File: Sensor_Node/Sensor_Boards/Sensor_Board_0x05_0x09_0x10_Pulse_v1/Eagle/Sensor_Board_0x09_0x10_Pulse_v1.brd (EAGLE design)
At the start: 55 x 35 mm, 21 parts, among them J3 1x3 RA Female .1", J4 ARDUINO_ISP, J6 1x3 RA Female .1", U2 ATMEGA328P_TQFP, Y1 8MHZ

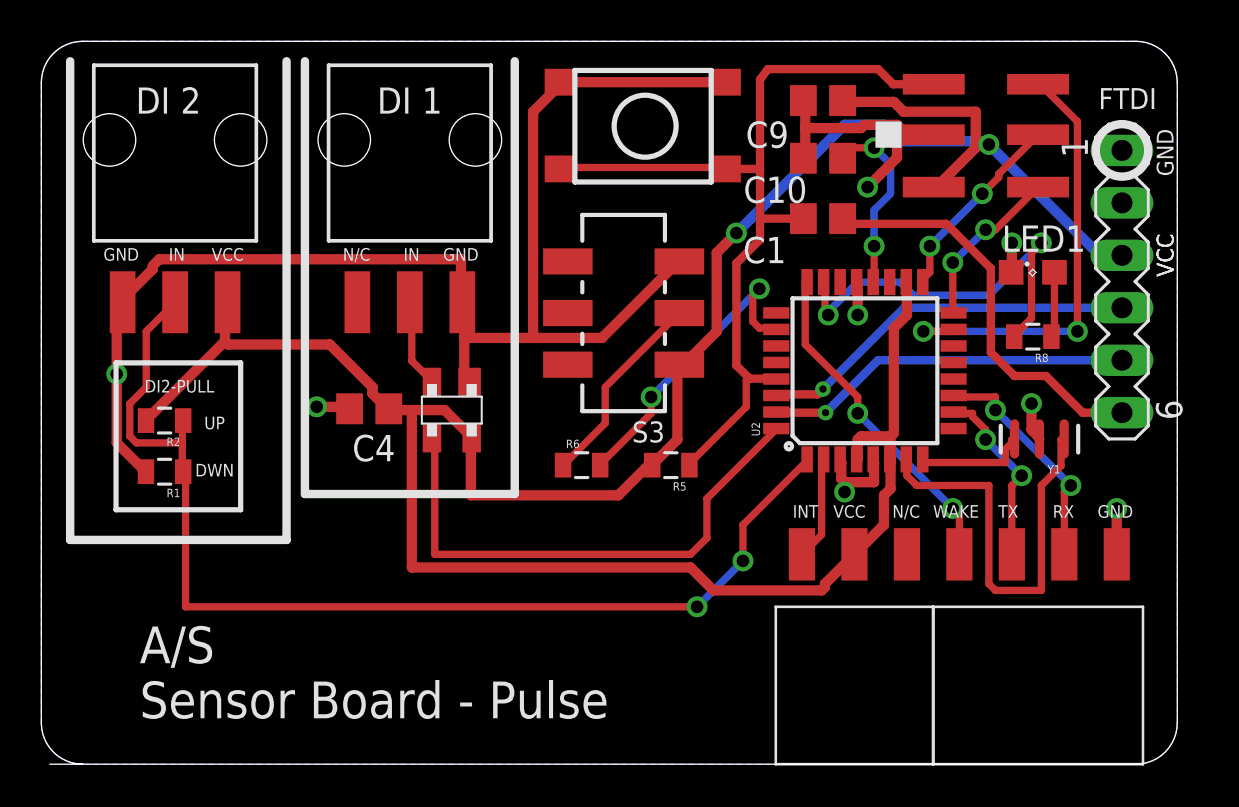
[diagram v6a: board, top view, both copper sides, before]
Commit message: Changes on PulseBoard
- startet replacement and rerouting
- corrected faulty VCC-Connection
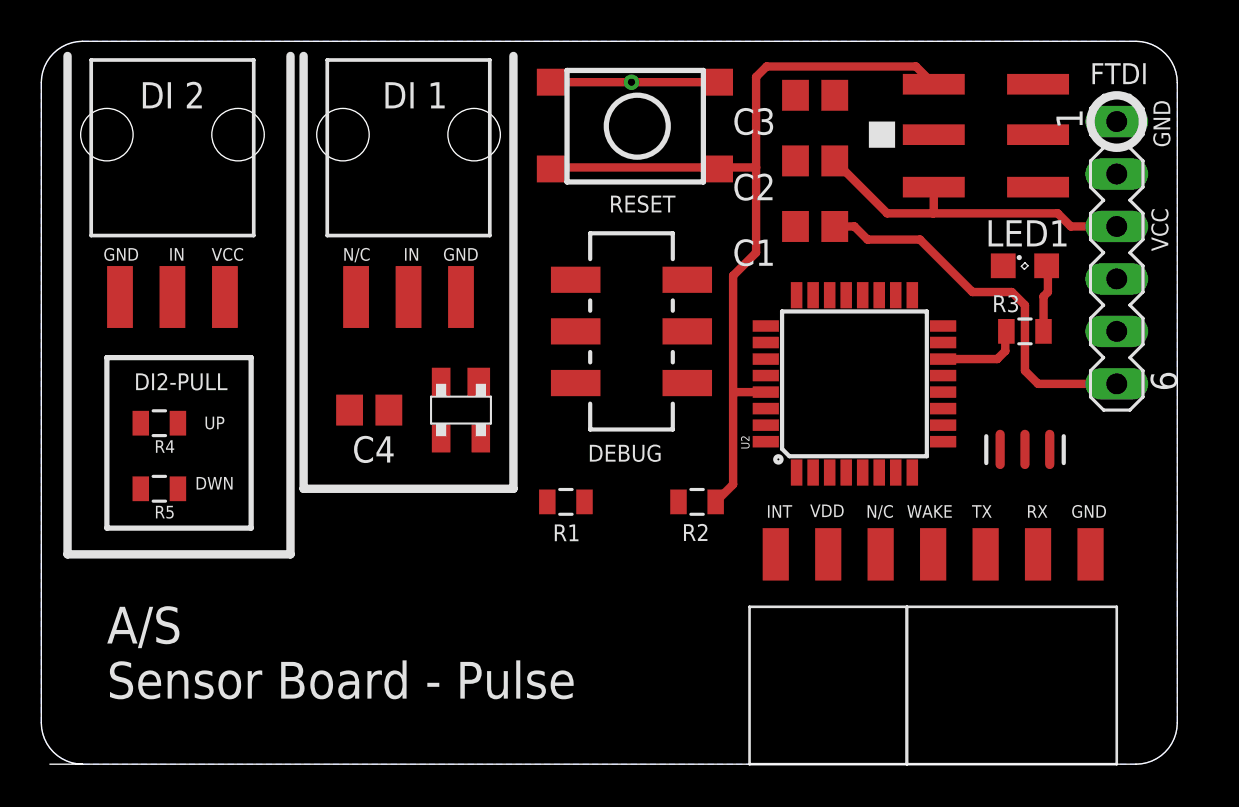
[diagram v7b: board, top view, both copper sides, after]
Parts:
- removed C10, C9: 100n, eagle-ltspice:C0805
- removed J3, J6: 1x3 RA Female .1", SparkFun-Connectors:1X03_SMD_RA_FEMALE
- removed R6: 10k, SparkFun-Passives:0805
- removed R8: 330, SparkFun-Passives:0805
- removed U$15: M03_SMD_90, myownthings:M03_SMD_90
- removed U$16: M04_SMD_90, myownthings:M04_SMD_90
- added C2, C3: 100n, eagle-ltspice:C0805
- added R3: 330, SparkFun-Passives:0805
- added R4: 10k, SparkFun-Passives:0805
- added SV2: M03_SMD_90, myownthings:M03_SMD_90
- added SV3: M04_SMD_90, myownthings:M04_SMD_90
- added SV4, SV5: 1x3 RA Female .1", SparkFun-Connectors:1X03_SMD_RA_FEMALE
- moved R2 26.1 mm to (31.8, 12.7)
- moved R5 24.8 mm to (5.71, 13.3)
- moved R1 19.5 mm to (25.4, 12.7), turned to 0 degrees
- moved SV1 1.42 mm to (52.1, 24.8)
- moved S3 0.97 mm to (28.6, 21.0)
- moved Y1 0.86 mm to (47.6, 15.2)
- moved U2 0.81 mm to (39.4, 18.4)
- moved C1 0.54 mm to (37.5, 26.0)
- moved LED1 0.50 mm to (47.6, 24.1)
- moved U$2 0.44 mm to (20.3, 17.1)
- moved S1 0.38 mm to (24.8, 33.0)
- moved C4 0.06 mm to (15.9, 17.1)
- renumbered J4 to SV6
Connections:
- new net VDD: C4.1, SV2.2, U$2.VCC
- net DBG_ENABLE: now also R1.2; no longer R6.2
- net DIGITAL_INPUT_2: now also R4.1, R5.1, SV5.2; no longer J3.2, R1.1, R2.1
- net GND: now also C2.2, C3.2, R5.2, SV3.4, SV4.1, SV5.3; no longer C10.2, C9.2, J3.3, J6.1, R1.2, U$16.4
- net INT_TO_COM: now also SV2.1; no longer U$15.1
- net L1: now also R3.2, U2.14; no longer R8.2, U2.23
- net MCU_RXI: now also SV3.3; no longer U$16.3
- net MCU_TXO: now also SV3.2; no longer U$16.2
- net N$15: now also C3.1; no longer C10.1
- net N$3: now also R1.1; no longer R6.1
- net N$30: now also R3.1; no longer R8.1
- net N$4: now also SV4.2; no longer J6.2
- net RESET: now also R2.1; no longer R5.1
- net VCC: now also C2.1, R4.2, SV5.1; no longer C4.1, C9.1, J3.1, R5.2, U$15.2, U$2.VCC
- net WAKE_UP: now also SV3.1; no longer U$16.1
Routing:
- net VCC: track 129.3 -> 16.3 mm, vias 2 -> 0
- net GND: track 92.3 -> 7.95 mm, vias 8 -> 1
- net DIGITAL_INPUT_2: track 53.3 -> 0.00 mm, vias 2 -> 0
- net DIGITAL_INPUT_1: track 25.9 -> 0.00 mm
- net MOSI: track 21.9 -> 0.00 mm, vias 2 -> 0
- net N$2: track 20.2 -> 0.00 mm
- net FTDI_RXI: track 18.5 -> 0.00 mm, vias 1 -> 0
- net FTDI_TXO: track 17.8 -> 0.00 mm, vias 1 -> 0
- net WAKE_UP: track 16.4 -> 0.00 mm, vias 2 -> 0
- net L1: track 19.2 -> 4.14 mm, vias 2 -> 0
- net DBG_ENABLE: track 14.8 -> 0.00 mm, vias 2 -> 0
- net MCU_RXI: track 11.3 -> 0.00 mm, vias 2 -> 0
- net N$3: track 9.70 -> 0.00 mm
- net SCK: track 9.44 -> 0.00 mm, vias 2 -> 0
- net N$15: track 9.17 -> 0.00 mm, vias 2 -> 0
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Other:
- board text added: "DEBUG"
- board text added: "RESET"
- board text added: "VDD"

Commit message: Finished Changes on PulseBoard
Pulseboard:
- tidied up routing and placement

TSL2561:
- tidied up some connections
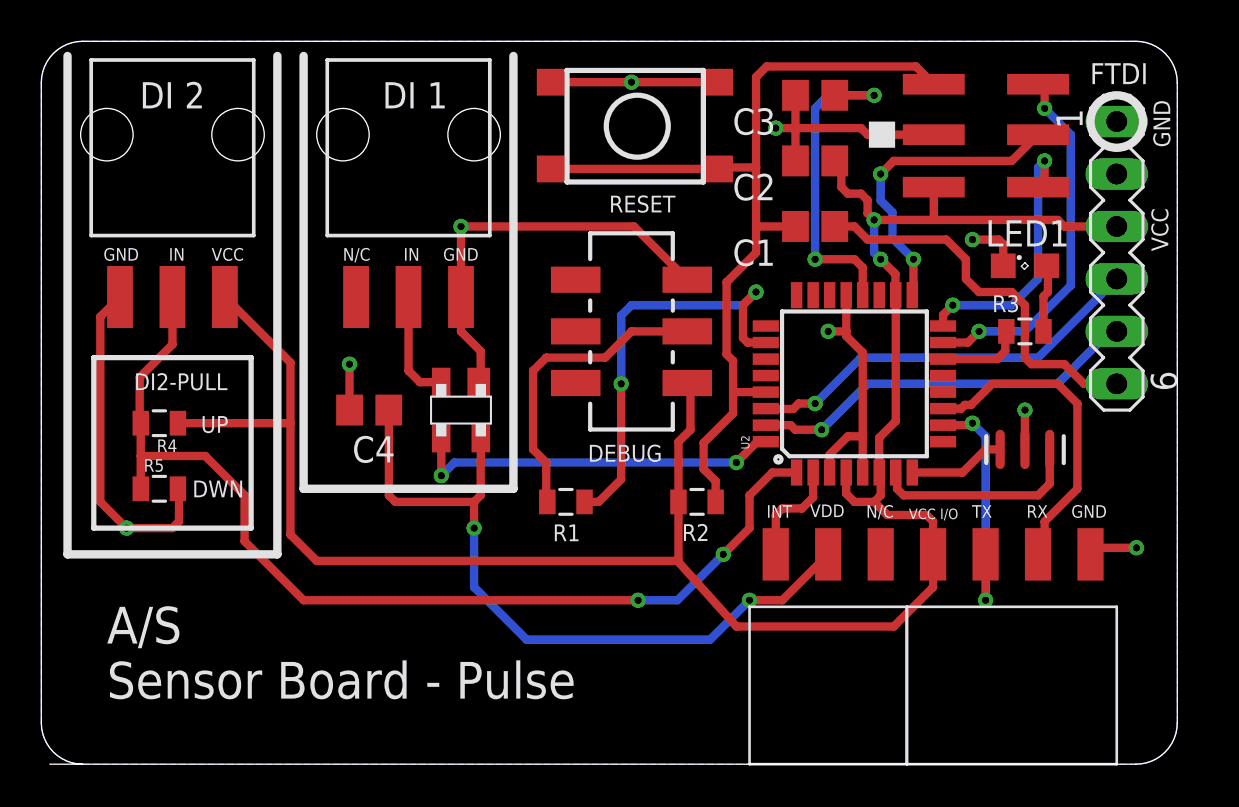
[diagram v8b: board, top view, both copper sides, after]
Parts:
- turned R4 to 0 degrees
- turned R5 to 0 degrees
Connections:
- removed net WAKE_UP: SV3.1, U2.24
- net VCC: now also SV3.1
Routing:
- net VCC: track 16.3 -> 102.1 mm, vias 0 -> 2
- net GND: track 7.95 -> 77.0 mm, vias 1 -> 9
- net DIGITAL_INPUT_2: track 0.00 -> 49.5 mm, vias 0 -> 2
- net VDD: track 0.00 -> 35.7 mm, vias 0 -> 2
- net DBG_ENABLE: track 0.00 -> 20.8 mm, vias 0 -> 2
- net FTDI_RXI: track 0.00 -> 19.6 mm, vias 0 -> 1
- net FTDI_TXO: track 0.00 -> 19.1 mm, vias 0 -> 1
- net DIGITAL_INPUT_1: track 0.00 -> 18.2 mm, vias 0 -> 2
- net MOSI: track 0.00 -> 17.7 mm, vias 0 -> 2
- net N$15: track 0.00 -> 16.1 mm, vias 0 -> 2
- net MCU_RXI: track 0.00 -> 15.5 mm
- net SCK: track 0.00 -> 15.0 mm, vias 0 -> 2
- net N$3: track 0.00 -> 14.9 mm
- net MISO: track 0.00 -> 13.1 mm, vias 0 -> 2
- net MCU_TXO: track 0.00 -> 12.5 mm, vias 0 -> 2
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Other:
- board text added: "VCC I/O"
- board text removed: "WAKE"
